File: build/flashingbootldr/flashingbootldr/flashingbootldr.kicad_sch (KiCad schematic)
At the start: 3 parts, among them U1 ATmega328P-P

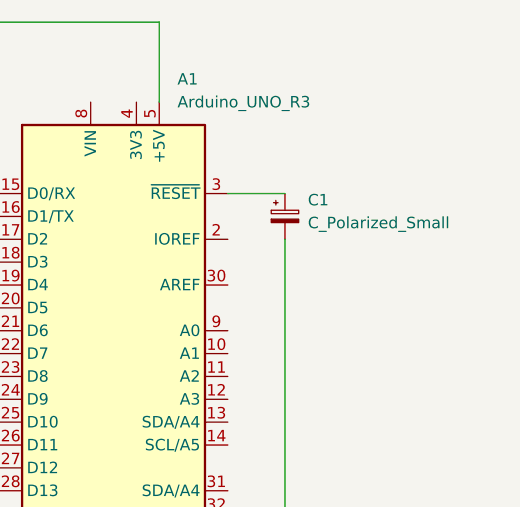
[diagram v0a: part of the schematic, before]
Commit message: update bootloader flashing instructions
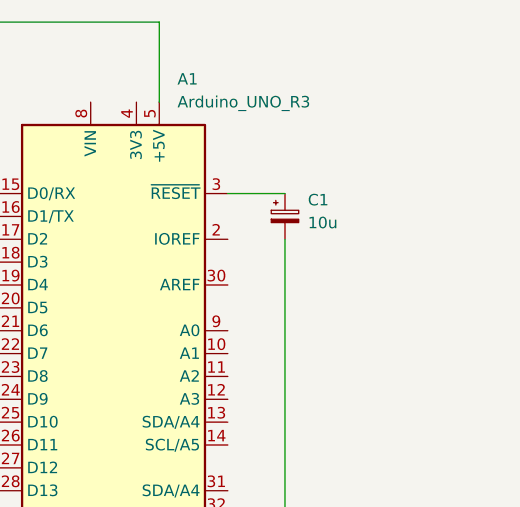
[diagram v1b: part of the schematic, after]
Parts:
- C1: value C_Polarized_Small -> 10u
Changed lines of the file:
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@@
       (effects (font (size 1.27 1.27)) (justify left))
     )
-    (property "Value" "C_Polarized_Small" (id 1) (at 242.57 76.9238 0)
+    (property "Value" "10u" (id 1) (at 242.57 76.9238 0)
       (effects (font (size 1.27 1.27)) (justify left))
     )
@@
     )
     (path "/e158f13d-5c0b-45f6-891f-0ce1aff2290a"
-      (reference "C1") (unit 1) (value "C_Polarized_Small") (footprint "Capacitor_THT:CP_Radial_D5.0mm_P2.50mm")
+      (reference "C1") (unit 1) (value "10u") (footprint "Capacitor_THT:CP_Radial_D5.0mm_P2.50mm")
     )
     (path "/7c87ef67-9e40-4b3f-8eaf-78a4e3eed88d"
